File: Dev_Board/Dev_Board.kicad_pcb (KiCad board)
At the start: 2 copper layers, 48.9 x 67.6 mm, 36 parts, among them J1 Conn_01x04, J2 Conn_01x04

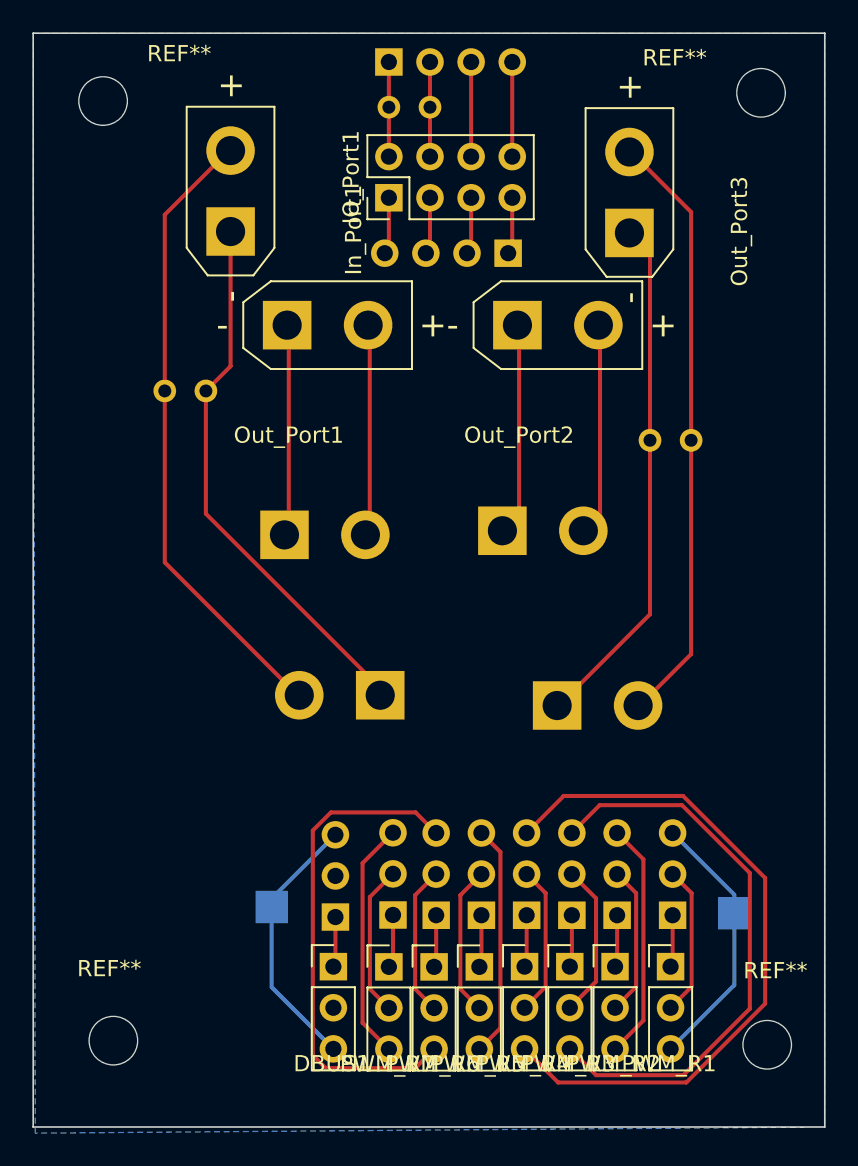
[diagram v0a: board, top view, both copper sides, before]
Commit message: Pass JLC DRC
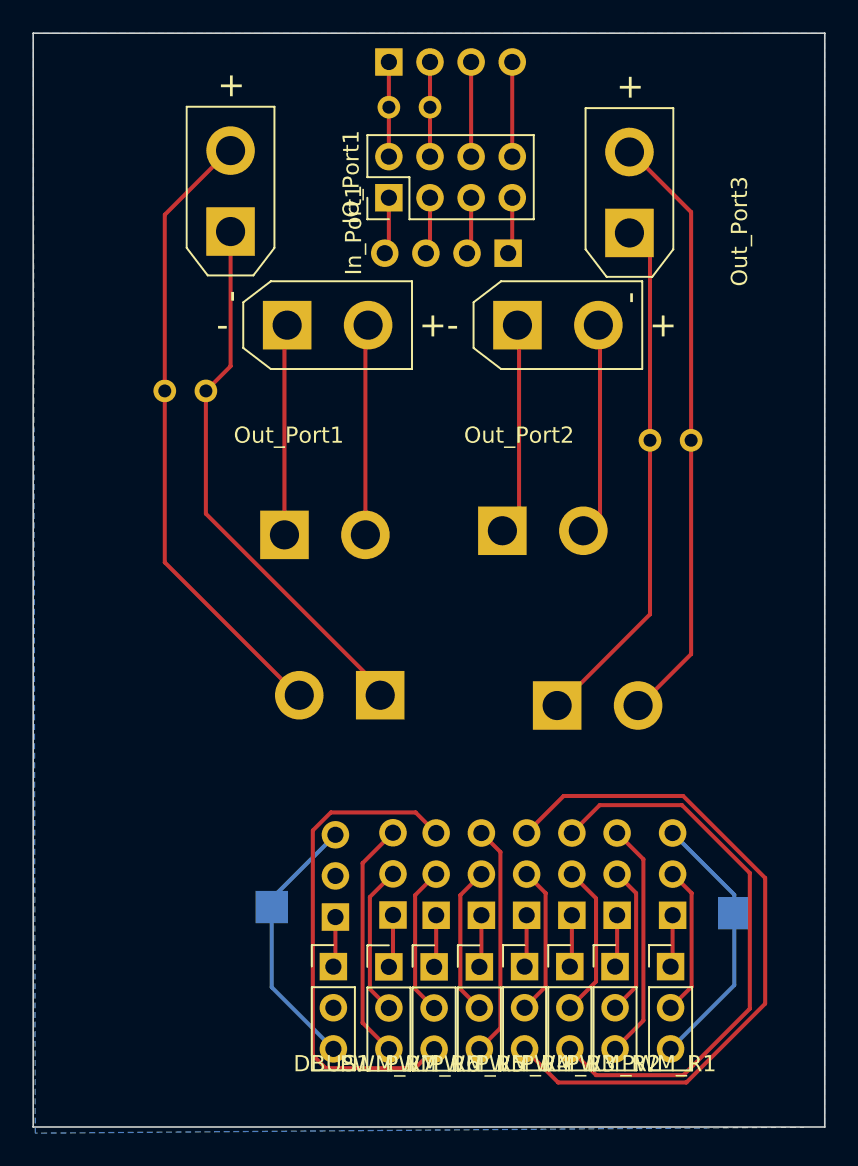
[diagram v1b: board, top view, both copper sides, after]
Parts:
- removed REF** (x4): MountingHole_3mm, MountingHole:MountingHole_3mm
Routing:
- net Net-(In_Port1-Pin_1): track 35.0 -> 33.7 mm
